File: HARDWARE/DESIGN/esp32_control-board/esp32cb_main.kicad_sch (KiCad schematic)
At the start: 17 parts, among them J10 ESP32-Prog, J11 RFID-module1, J12 RFID-module2, SW301 Reset, SW302 Boot, U1 ESP32-S3-WROOM-1

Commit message: 60710 - schematic and PCB-layout updated
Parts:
- removed J10: ESP32-Prog, Connector_PinHeader_2.54mm:PinHeader_1x04_P2.54mm_Vertical, symbol Connector:Screw_Terminal_01x04
- removed R304: 10k, Resistor_SMD:R_0603_1608Metric, symbol Device:R
- added C318, C319, C320, C321: 100n, Capacitor_SMD:C_0603_1608Metric, symbol Device:C
- added D15: MCU ok, LED_SMD:LED_0603_1608Metric, symbol Device:LED
- added J301: USB-Prog, (FOOTPRINTS):C3151749_USB_TYPE-C_Vertical, symbol Connector:USB_C_Receptacle_USB2.0
- added J302: UART-Prog, (FOOTPRINTS):C3151749_USB_TYPE-C_Vertical, symbol Connector:USB_C_Receptacle_USB2.0
- added Q4, Q5: SS8050, Package_TO_SOT_SMD:SOT-23, symbol Transistor_BJT:SS8050
- added R10: 1k, Resistor_SMD:R_0603_1608Metric, symbol Device:R
- added R306, R341, R342: 12k, Resistor_SMD:R_0603_1608Metric, symbol Device:R
- added R309, R310, R338, R339: 5k1, Resistor_SMD:R_0603_1608Metric, symbol Device:R
- added U17: CH343P, Package_DFN_QFN:TQFN-16-1EP_3x3mm_P0.5mm_EP1.23x1.23mm, symbol CPLA_global_kicad_library:CH343P
- added U302, U303: USBLC6-2SC6, Package_TO_SOT_SMD:SOT-23-6, symbol Power_Protection:USBLC6-2SC6
- R305: value 10k -> 12k; LCSC (none) -> C2907097; LCSC part C25804 -> (none); Manufacturer UNI-ROYAL -> FOJAN; Property 1% -> 5%
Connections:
- net +3V3: now also C319.2, R306.1, U17.1 (VIO)
- net GND: now also C318.1, C319.1, C320.1, C321.1, D15.1 (K), J301.A1 (GND), J301.A12 (GND), J301.B1 (GND), J301.B12 (GND), J301.S1 (SHIELD), J302.A1 (GND), J302.A12 (GND), J302.B1 (GND), J302.B12 (GND), J302.S1 (SHIELD), R309.1, R310.1, R338.1, R339.1, U17.17 (GND), U17.2 (GND), U302.2 (GND), U303.2 (GND)
- net esp_Boot: now also Q5.3 (C)
- net esp_Reset: now also Q4.3 (C), R306.2
- net esp_LED: now reaches U1.39 (IO1)
- net esp_LED: now also R10.1
- net espM_USB_d+ renamed espU_USB_d+
- net espU_USB_d+: now also U302.1 (I/O1)
- net espM_USB_d- renamed espU_USB_d-
- net espU_USB_d-: now also U302.3 (I/O2)
- net esp_Rx renamed esp_RXD
- net esp_RXD: now also U17.4 (TXD)
- net esp_Tx renamed esp_TXD
- net esp_TXD: now also U17.5 (RXD)
- new net: J302.A5 (CC1), R339.2
- new net: J302.B5 (CC2), R338.2
- new net: J301.B5 (CC2), R309.2
- new net: D15.2 (A), R10.2
- new net: Q5.1 (B), R342.2
- new net: J301.A5 (CC1), R310.2
- new net: C321.2, U17.6 (V3)
- new net: Q4.1 (B), R341.2
- new net +5V_usb: U302.5 (VBUS), U303.5 (VBUS)
- new net DTR: Q5.2 (E), R341.1, U17.12 (DTR)
- new net RTS: Q4.2 (E), R342.1, U17.13 (RTS)
- new net Vusb: C318.2, C320.2, J301.A4 (VBUS), J301.A9 (VBUS), J301.B4 (VBUS), J301.B9 (VBUS), J302.A4 (VBUS), J302.A9 (VBUS), J302.B4 (VBUS), J302.B9 (VBUS), U17.3 (VDD), U17.9 (VBUS)
- new net espS_USB_d+: U17.7 (UD+), U303.6 (I/O1)
- new net espS_USB_d-: U17.8 (UD-), U303.4 (I/O2)
- new net espS_USB_dm: J302.A7 (D-), J302.B7 (D-), U303.3 (I/O2)
- new net espS_USB_dp: J302.A6 (D+), J302.B6 (D+), U303.1 (I/O1)
- new net espU_USB_dm: J301.A7 (D-), J301.B7 (D-), U302.4 (I/O2)
- new net espU_USB_dp: J301.A6 (D+), J301.B6 (D+), U302.6 (I/O1)
- no-connect marks 5 -> 14
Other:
- note added: "Auto-reset/flash switch circuit"
- note added: "USB-UART bridge"
- moved on the sheet: C301, C302, R303, R308, R336, R337, U1

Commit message: 60714 - one of two I2C-mux ICs was removed, PCB-layout finished, start tracing
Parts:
- J204: renamed from J302; value UART-Prog -> UART-Debug
- renumbered C303 to C201, C314 to C202, C315 to C203, C319 to C204, C320 to C205, C321 to C206, C318 to C207, C301 to C208, C302 to C209, D15 to D201, J11 to J201, J12 to J202, J301 to J203, Q4 to Q201, Q5 to Q202, R305 to R201, R306 to R202, R309 to R203, R336 to R204, R310 to R205, R337 to R206, R338 to R207, R339 to R208, R341 to R209, R342 to R210, R303 to R211, R308 to R212, R10 to R213, SW302 to SW201, SW301 to SW202, U17 to U201, U302 to U202, U1 to U203, U303 to U204
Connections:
- net GPIO40 is gone; now on net LOCK8_signal: U203.33 (IO40)
- net GPIO41 is gone; now on net LOCK7_signal: U203.34 (IO41)
- net GPIO42 is gone; now on net LOCK6_signal: U203.35 (IO42)
- net LOCK1_signal: now also U203.4 (IO4)
- net LOCK2_signal: now also U203.5 (IO5)
- net LOCK3_signal: now also U203.6 (IO6)
- net LOCK4_signal: now also U203.7 (IO7)
- net LOCK5_signal: now also U203.38 (IO2)
- net RFID1_irq: now also U203.8 (IO15)
- net RFID1_reset: now also U203.9 (IO16)
- net RFID2_irq: now also U203.29 (IO36)
- net RFID2_reset: now also U203.28 (IO35)
- net SPI_cs2: now also U203.30 (IO37)
- net LOCK6_do: now reaches U203.22 (IO14)
- net GPIO17 renamed LOCK7_do
- net GPIO18 renamed LOCK8_do
- net GPIO21 renamed LOCK5_do
- net GPIO38 renamed LOCK2_do
- net GPIO39 renamed LOCK1_do
- net GPIO47 renamed LOCK4_do
- net GPIO48 renamed LOCK3_do
- no-connect marks 14 -> 12
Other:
- moved on the sheet: C202, C203, J201, J202, J204, R207, R208, U204

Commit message: 60714 - traced 20%
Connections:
- net +5V_usb is gone; now on net Vusb: U202.5 (VBUS), U204.5 (VBUS)
- net RFID1_irq: now also U203.9 (IO16); no longer U203.8 (IO15)
- net RFID1_reset: now also U203.8 (IO15); no longer U203.9 (IO16)

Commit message: 60714 - traced 25%
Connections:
- net GND: no longer U203.1 (GND), U203.40 (GND), U203.41 (GND)
- new net GND_MCU: U203.1 (GND), U203.40 (GND), U203.41 (GND)
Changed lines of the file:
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@@
+	)
+	(symbol
+		(lib_id "power:GND")
+		(at 219.71 111.76 0)
+		(mirror y)
+		(unit 1)
+		(body_style 1)
+		(exclude_from_sim no)
+		(in_bom yes)
+		(on_board yes)
+		(in_pos_files yes)
+		(dnp no)
+		(property "Reference" "#PWR0461"
+			(at 219.71 118.11 0)
+			(hide yes)
+			(show_name no)
+			(do_not_autoplace no)
+			(effects
+				(font
+					(size 1.27 1.27)
+				)
+			)
+		)
+		(property "Value" "GND_MCU"
+			(at 219.71 116.84 0)
+			(show_name no)
+			(do_not_autoplace no)
+			(effects
+				(font
+					(size 1.27 1.27)
+				)
+			)
+		)
+		(property "Footprint" ""
+			(at 219.71 111.76 0)
+			(hide yes)
+			(show_name no)
+			(do_not_autoplace no)
+			(effects
+				(font
+					(size 1.27 1.27)
+				)
+			)
+		)
+		(property "Datasheet" ""
+			(at 219.71 111.76 0)
+			(hide yes)
+			(show_name no)
+			(do_not_autoplace no)
+			(effects
+				(font
+					(size 1.27 1.27)
+				)
+			)
+		)
+		(property "Description" ""
+			(at 219.71 111.76 0)
+			(show_name no)
+			(do_not_autoplace no)
+			(effects
+				(font
+					(size 1.27 1.27)
+				)
+			)
+		)
+		(property "LCSC" ""
+			(at 219.71 111.76 0)
+			(hide yes)
+			(show_name no)
+			(do_not_autoplace no)
+			(effects
+				(font
+					(size 1.27 1.27)
+				)
+			)
+		)
+		(property "Manufacturer" ""
+			(at 219.71 111.76 0)
+			(hide yes)
+			(show_name no)
+			(do_not_autoplace no)
+			(effects
+				(font
+					(size 1.27 1.27)
+				)
+			)
+		)
+		(property "Package" ""
+			(at 219.71 111.76 0)
+			(show_name no)
+			(do_not_autoplace no)
+			(effects
+				(font
+					(size 1.27 1.27)
+				)
+			)
+		)
+		(property "Property" ""
+			(at 219.71 111.76 0)
+			(show_name no)
+			(do_not_autoplace no)
+			(effects
+				(font
+					(size 1.27 1.27)
+				)
+			)
+		)
+		(pin "1"
+		)
+		(instances
+			(project "esp32_control-board"
+				(path "/71812bfc-9597-4f26-a67f-4f6ff697416c/b211aa99-c245-41c6-9b64-a229e59ffb83"
+					(reference "#PWR0461")
+					(unit 1)
+				)
+			)
+		)
 	)
 	(symbol
@@
 					(unit 1)
 				)
-			)
-		)
-	)
-	(symbol
-		(lib_id "power:GND")
-		(at 219.71 111.76 0)
-		(unit 1)
-		(body_style 1)
-		(exclude_from_sim no)
-		(in_bom yes)
-		(on_board yes)
-		(in_pos_files yes)
-		(dnp no)
-		(property "Reference" "#PWR0234"
-			(at 219.71 118.11 0)
-			(hide yes)
-			(show_name no)
-			(do_not_autoplace no)
-			(effects
-				(font
-					(size 1.27 1.27)
-				)
-			)
-		)
-		(property "Value" "GND"
-			(at 219.71 116.84 0)
-			(show_name no)
-			(do_not_autoplace no)
-			(effects
-				(font
-					(size 1.27 1.27)
-				)
-			)
-		)
-		(property "Footprint" ""
-			(at 219.71 111.76 0)
-			(hide yes)
-			(show_name no)
-			(do_not_autoplace no)
-			(effects
-				(font
-					(size 1.27 1.27)
-				)
-			)
-		)
-		(property "Datasheet" ""
-			(at 219.71 111.76 0)
-			(hide yes)
-			(show_name no)
-			(do_not_autoplace no)
-			(effects
-				(font
-					(size 1.27 1.27)
-				)
-			)
-		)
-		(property "Description" ""
-			(at 219.71 111.76 0)
-			(show_name no)
-			(do_not_autoplace no)
-			(effects
-				(font
-					(size 1.27 1.27)
-				)
-			)
-		)
-		(pin "1"
-		)
-		(instances
-			(project "esp32_control-board"
-				(path "/71812bfc-9597-4f26-a67f-4f6ff697416c/b211aa99-c245-41c6-9b64-a229e59ffb83"
-					(reference "#PWR0234")
-					(unit 1)
-				)

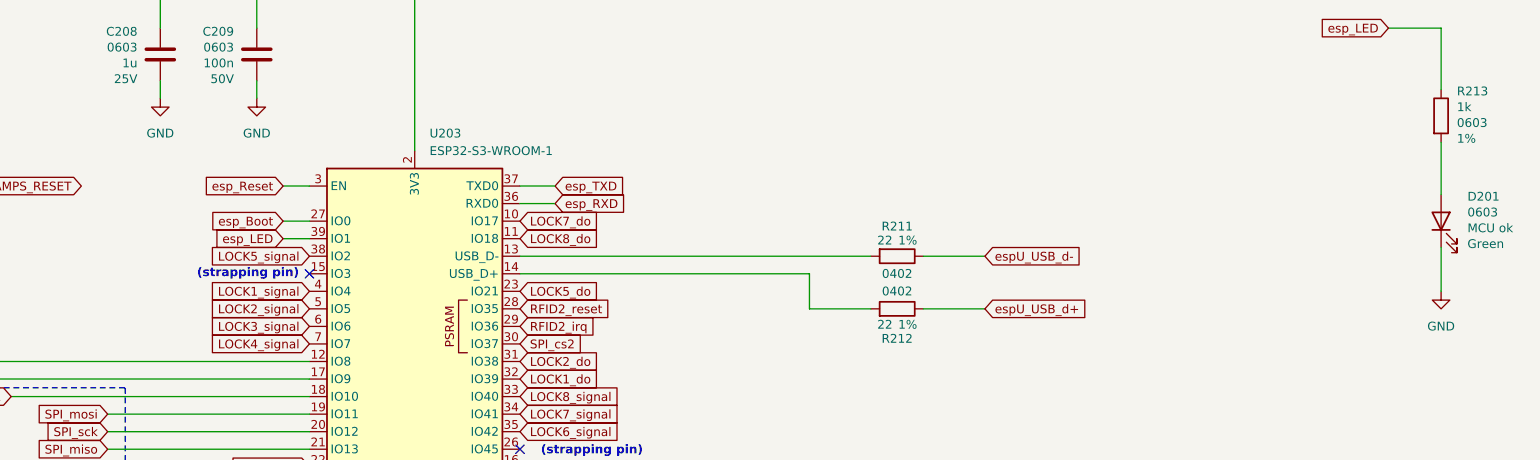
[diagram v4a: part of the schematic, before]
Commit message: 60715 - traced 75%
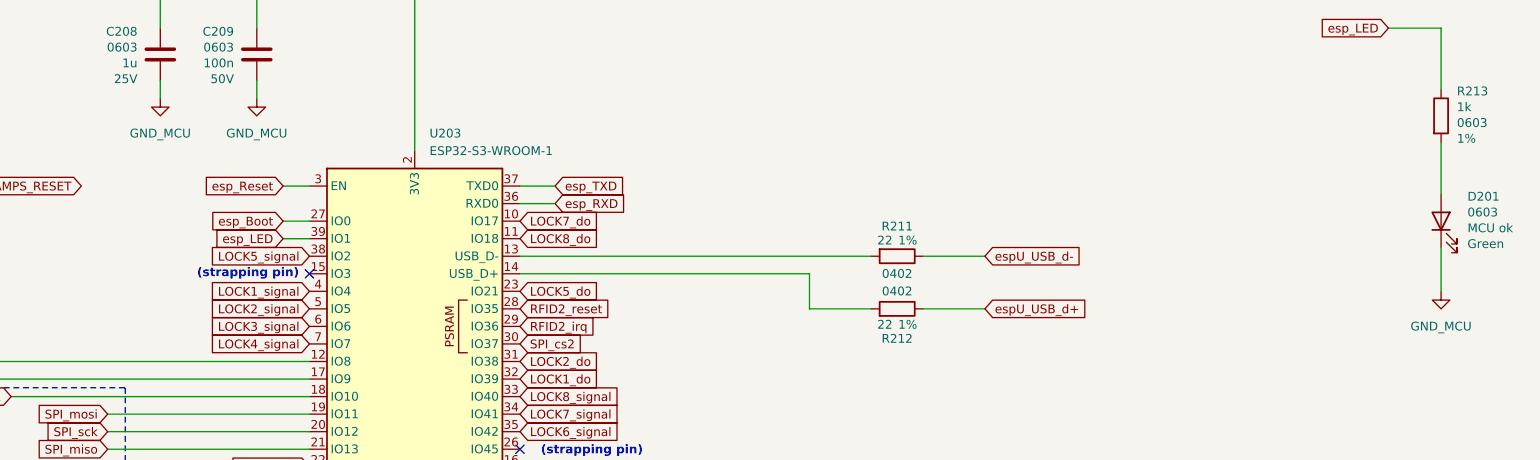
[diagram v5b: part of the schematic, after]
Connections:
- net GND: no longer C208.1, C209.1, D201.1 (K)
- net GND_MCU: now also C208.1, C209.1, D201.1 (K)

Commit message: 60821 - Schematic is under reconstruction for ver.2
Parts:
- added D202: MCU ok, LED_SMD:LED_0603_1608Metric, symbol Device:LED
- added R214: 1k, Resistor_SMD:R_0603_1608Metric, symbol Device:R
- J204: value UART-Debug -> USB-prog
- U203: value ESP32-S3-WROOM-1 -> ESP32-S3-WROOM-1U; footprint RF_Module:ESP32-S3-WROOM-1 -> RF_Module:ESP32-S3-WROOM-1U; LCSC (none) -> C3013946; Manufacturer (none) -> ESPRESSIF; Package (none) -> Ext.antenna
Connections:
- net GND_MCU: now also D202.1 (K)
- net LOCK1_do: no longer names the net of U203.32 (IO39)
- net LOCK1_signal: no longer names the net of U203.4 (IO4)
- net LOCK2_do: no longer names the net of U203.31 (IO38)
- net LOCK2_signal: no longer names the net of U203.5 (IO5)
- net LOCK3_do: no longer names the net of U203.25 (IO48)
- net LOCK3_signal: no longer names the net of U203.6 (IO6)
- net LOCK4_do: no longer names the net of U203.24 (IO47)
- net LOCK4_signal: no longer names the net of U203.7 (IO7)
- net LOCK5_do: no longer names the net of U203.23 (IO21)
- net LOCK5_signal: no longer names the net of U203.38 (IO2)
- net LOCK6_do: no longer names the net of U203.22 (IO14)
- net LOCK6_signal: no longer names the net of U203.35 (IO42)
- net LOCK7_do: no longer names the net of U203.10 (IO17)
- net LOCK7_signal: no longer names the net of U203.34 (IO41)
- net LOCK8_do: no longer names the net of U203.11 (IO18)
- net LOCK8_signal: no longer names the net of U203.33 (IO40)
- net esp_LED renamed esp_LED_green
- new net: D202.2 (A), R214.2
- new net esp_LED_red: R214.1
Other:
- moved on the sheet: D201, R213

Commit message: 60825 - Schematic update and PCB-layout started
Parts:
- removed C202, C203: 1u, Capacitor_SMD:C_0603_1608Metric, symbol Device:C
- removed C204, C205, C206, C207: 100n, Capacitor_SMD:C_0603_1608Metric, symbol Device:C
- removed J201: RFID-module1, Connector_JST:JST_PH_B8B-PH-K_1x08_P2.00mm_Vertical, symbol Connector:Screw_Terminal_01x08
- removed J202: RFID-module2, Connector_JST:JST_PH_B8B-PH-K_1x08_P2.00mm_Vertical, symbol Connector:Screw_Terminal_01x08
- removed J203: USB-Prog, (FOOTPRINTS):C3151749_USB_TYPE-C_Vertical, symbol Connector:USB_C_Receptacle_USB2.0
- removed Q201, Q202: SS8050, Package_TO_SOT_SMD:SOT-23, symbol Transistor_BJT:SS8050
- removed R201, R202, R209, R210: 12k, Resistor_SMD:R_0603_1608Metric, symbol Device:R
- removed R203, R205: 5k1, Resistor_SMD:R_0603_1608Metric, symbol Device:R
- removed U201: CH343P, Package_DFN_QFN:TQFN-16-1EP_3x3mm_P0.5mm_EP1.23x1.23mm, symbol CPLA_global_kicad_library:CH343P
- removed U202: USBLC6-2SC6, Package_TO_SOT_SMD:SOT-23-6, symbol Power_Protection:USBLC6-2SC6
- added C210: 100n, Capacitor_SMD:C_0603_1608Metric, symbol Device:C
- added C217: 1u, Capacitor_SMD:C_0603_1608Metric, symbol Device:C
- added D203: XL-1608UBC-06A, LED_SMD:LED_0603_1608Metric, symbol Device:LED
- added D204: XL-1608SURUGC, LED_SMD:LED_0603_1608Metric, symbol Device:LED
- added R109, R110: 12k, Resistor_SMD:R_0603_1608Metric, symbol Device:R
- added R120: 1M, Resistor_SMD:R_0603_1608Metric, symbol Device:R
- added R121: 270k, Resistor_SMD:R_0603_1608Metric, symbol Device:R
- C208: value 1u -> 22u; footprint Capacitor_SMD:C_0603_1608Metric -> Capacitor_SMD:C_0805_2012Metric; LCSC (none) -> C907991; LCSC part C29936 -> (none); Manufacturer Samsung Electro-Mechanics -> muRata; Property 25V -> 10V
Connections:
- net espU_USB_d+ is gone; now on net esp_USB_d+: R212.1
- net espU_USB_d- is gone; now on net esp_USB_d-: R211.1
- net +3V3: now also R109.1, R110.1
- net GND: now also C210.1, R121.2
- net esp_Boot: now also R109.2
- net esp_Reset: now also R110.2
- net TWAI_TX: now reaches U203.4 (IO4)
- net TWAI_RX: now reaches U203.5 (IO5)
- net esp_ADC1_ch5: now reaches U203.6 (IO6)
- net esp_ADC1_ch6: now reaches U203.7 (IO7)
- net RFID2_irq: no longer names the net of U203.29 (IO36)
- net RFID2_reset: no longer names the net of U203.28 (IO35)
- net SPI_cs2: no longer names the net of U203.30 (IO37)
- net espS_USB_d+ renamed esp_USB_d-
- net espS_USB_d- renamed esp_USB_d+
- net espS_USB_dm renamed esp_USB_dN
- net esp_USB_dN: now also U204.1 (I/O1); no longer U204.3 (I/O2)
- net espS_USB_dp renamed esp_USB_dP
- net esp_USB_dP: now also U204.3 (I/O2); no longer U204.1 (I/O1)
- new net +12V: R120.1
- new net ai_BatteryVoltage: C210.2, R120.2, R121.1
- no-connect marks 12 -> 8
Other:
- note added: "Battery-voltage measurement circuit"
- note added: "MCU"
- note added: "Manual controls"
- note added: "USB-interface"
- note removed: "Auto-reset/flash switch circuit"
- note removed: "USB-UART bridge"
- moved on the sheet: C201, C208, C209, D201, D202, J204, R204, R206, R207, R208, R211, R212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

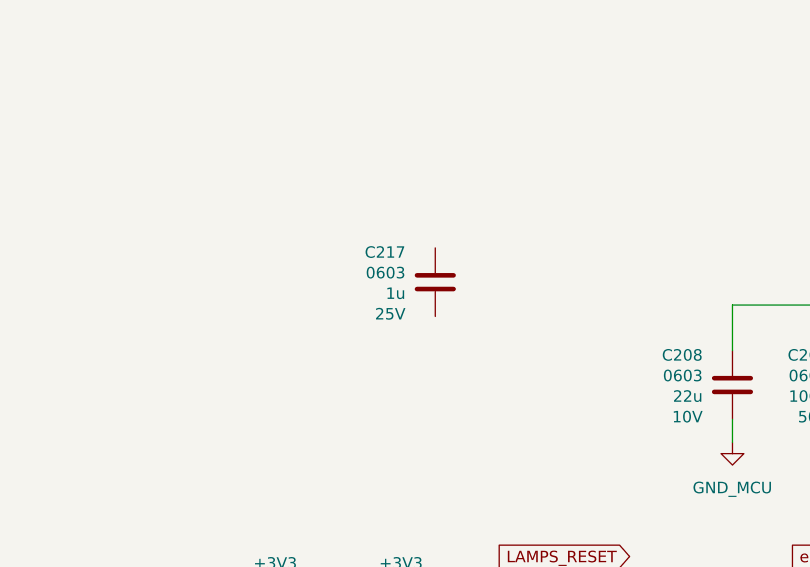
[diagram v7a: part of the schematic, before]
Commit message: 60828 - Schematic updated, preliminary PCB-layout done
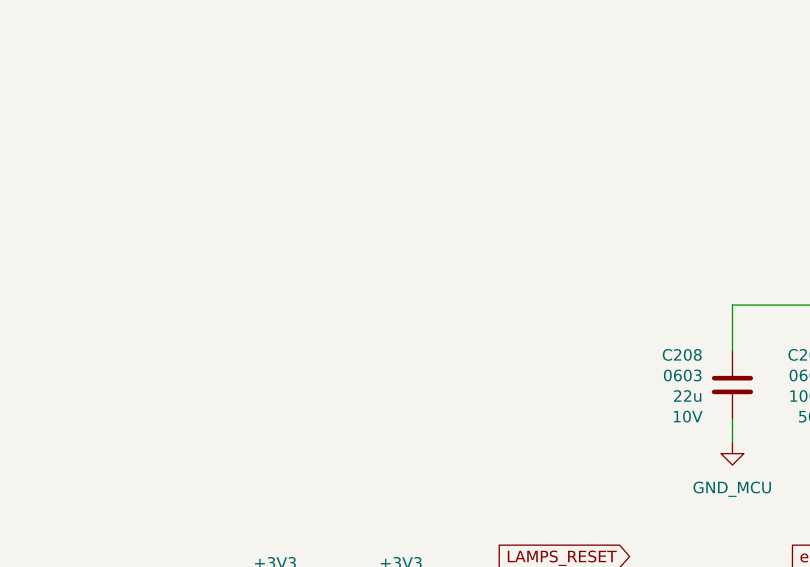
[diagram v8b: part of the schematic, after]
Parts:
- removed C217: 1u, Capacitor_SMD:C_0603_1608Metric, symbol Device:C
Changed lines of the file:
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@@
 	(title_block
 		(title "ESP32-based Control Board")
-		(date "2026-08-25")
+		(date "2026-08-28")
 		(rev "2a")
 	)
@@
 					(unit 1)
 				)
-			)
-		)
-	)
-	(symbol
-		(lib_id "Device:C")
-		(at 91.44 57.15 0)
-		(mirror x)
-		(unit 1)
-		(body_style 1)
-		(exclude_from_sim no)
-		(in_bom yes)
-		(on_board yes)
-		(in_pos_files yes)
-		(dnp no)
-		(property "Reference" "C217"
-			(at 88.138 53.848 0)
-			(show_name no)
-			(do_not_autoplace no)
-			(effects
-				(font
-					(size 1.27 1.27)
-				)
-				(justify right)
-			)
-		)
-		(property "Value" "1u"
-			(at 88.138 58.42 0)
-			(show_name no)
-			(do_not_autoplace no)
-			(effects
-				(font
-					(size 1.27 1.27)
-				)
-				(justify right)
-			)
-		)
-		(property "Footprint" "Capacitor_SMD:C_0603_1608Metric"
-			(at 92.4052 53.34 0)
-			(hide yes)
-			(show_name no)
-			(do_not_autoplace no)
-			(effects
-				(font
-					(size 1.27 1.27)
-				)
-			)
-		)
-		(property "Datasheet" ""
-			(at 91.44 57.15 0)
-			(hide yes)
-			(show_name no)
-			(do_not_autoplace no)
-			(effects
-				(font
-					(size 1.27 1.27)
-				)
-			)
-		)
-		(property "Description" ""
-			(at 91.44 57.15 0)
-			(show_name no)
-			(do_not_autoplace no)
-			(effects
-				(font
-					(size 1.27 1.27)
-				)
-			)
-		)
-		(property "LCSC part" "C29936"
-			(at 91.44 57.15 0)
-			(hide yes)
-			(show_name no)
-			(do_not_autoplace no)
-			(effects
-				(font
-					(size 1.27 1.27)
-				)
-			)
-		)
-		(property "Manufacturer" "Samsung Electro-Mechanics"
-			(at 91.44 57.15 0)
-			(hide yes)
-			(show_name no)
-			(do_not_autoplace no)
-			(effects
-				(font
-					(size 1.27 1.27)
-				)
-			)
-		)
-		(property "Package" "0603"
-			(at 88.138 56.134 0)
-			(show_name no)
-			(do_not_autoplace no)
-			(effects
-				(font
-					(size 1.27 1.27)
-				)
-				(justify right)
-			)
-		)
-		(property "Property" "25V"
-			(at 88.138 60.706 0)
-			(show_name no)
-			(do_not_autoplace no)
-			(effects
-				(font
-					(size 1.27 1.27)
-				)
-				(justify right)
-			)
-		)
-		(property "LCSC" ""
-			(at 91.44 57.15 0)
-			(hide yes)
-			(show_name no)
-			(do_not_autoplace no)
-			(effects
-				(font
-					(size 1.27 1.27)
-				)
-			)
-		)
-		(pin "1"
-		)
-		(pin "2"
-		)
-		(instances
-			(project "esp32_control-board"
-				(path "/71812bfc-9597-4f26-a67f-4f6ff697416c/b211aa99-c245-41c6-9b64-a229e59ffb83"
-					(reference "C217")
-					(unit 1)
-				)
